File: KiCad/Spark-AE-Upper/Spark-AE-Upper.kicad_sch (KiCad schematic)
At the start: 16 parts, among them J1 SSM-120-L-SV-BE, J2 SSM-120-L-SV-BE, J3 Conn_02x05_Odd_Even, J4 Conn_02x05_Odd_Even, J5 Conn_01x08_Socket, J6 Conn_01x08_Socket, J7 USB_C_Receptacle, J8 Micro_SD_Card_Det1, SW1 SW_Push, SW2 SW_Push

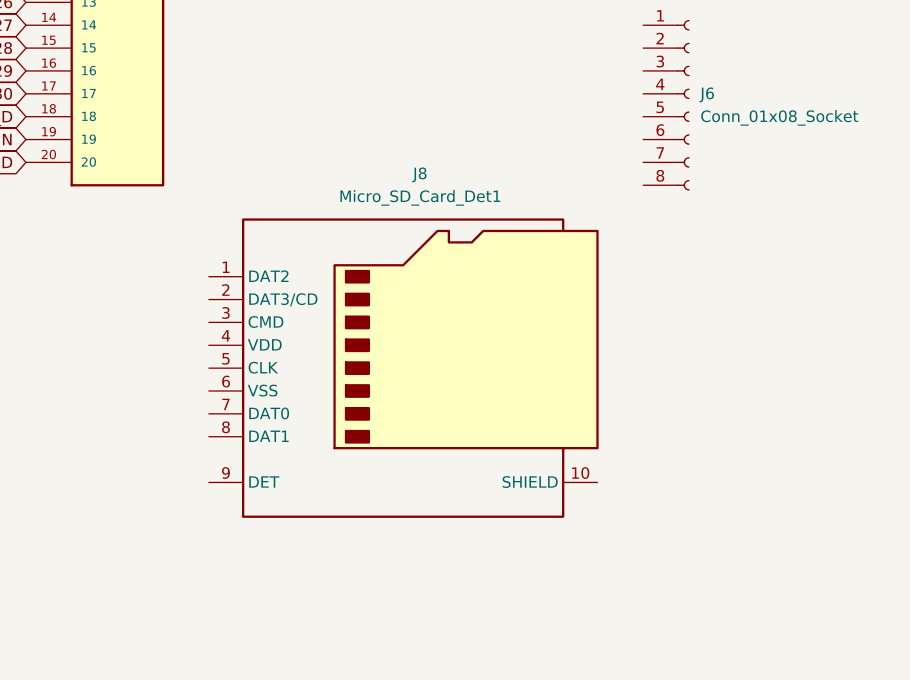
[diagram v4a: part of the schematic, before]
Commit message: updated footprints and models
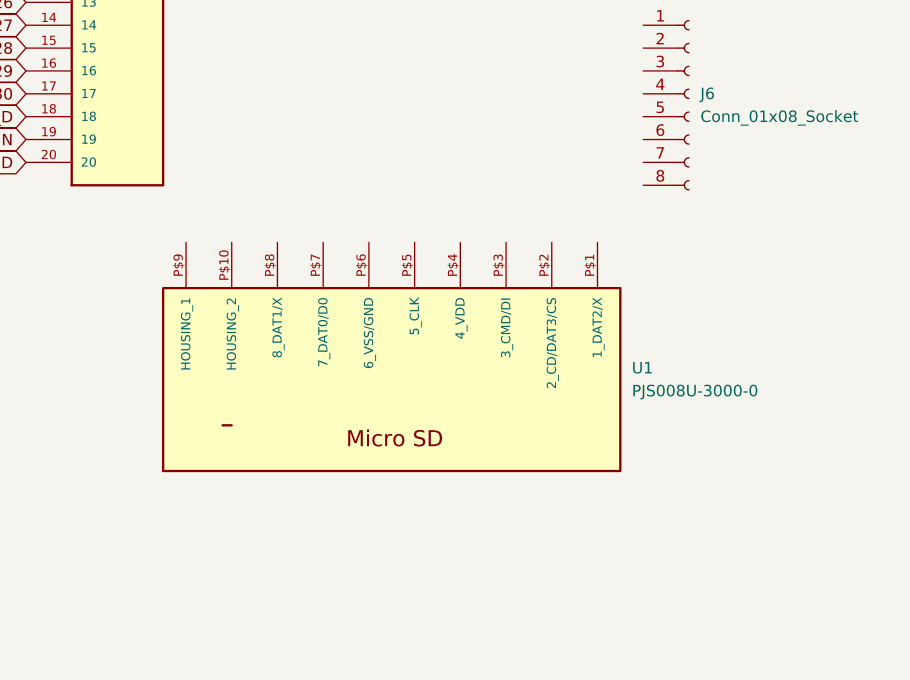
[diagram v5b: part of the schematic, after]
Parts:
- removed J8: Micro_SD_Card_Det1, Connector_Card:microSD_HC_Molex_104031-0811, symbol Connector:Micro_SD_Card_Det1
- added U1: PJS008U-3000-0, clectric-diy:PJS008U-3000-0, symbol clectric-diy:PJS008U-3000-0
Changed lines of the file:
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@@
+	)
+	(symbol
+		(lib_id "clectric-diy:PJS008U-3000-0")
+		(at 227.33 147.32 0)
+		(unit 1)
+		(exclude_from_sim no)
+		(in_bom yes)
+		(on_board yes)
+		(dnp no)
+		(fields_autoplaced yes)
+		(property "Reference" "U1"
+			(at 254 146.0499 0)
+			(effects
+				(font
+					(size 1.27 1.27)
+				)
+				(justify left)
+			)
+		)
+		(property "Value" "PJS008U-3000-0"
+			(at 254 148.5899 0)
+			(effects
+				(font
+					(size 1.27 1.27)
+				)
+				(justify left)
+			)
+		)
+		(property "Footprint" "clectric-diy:PJS008U-3000-0"
+			(at 227.33 147.32 0)
+			(effects
+				(font
+					(size 1.27 1.27)
+				)
+				(justify bottom)
+				(hide yes)
+			)
+		)
+		(property "Datasheet" ""
+			(at 227.33 147.32 0)
+			(effects
+				(font
+					(size 1.27 1.27)
+				)
+				(hide yes)
+			)
+		)
+		(property "Description" ""
+			(at 227.33 147.32 0)
+			(effects
+				(font
+					(size 1.27 1.27)
+				)
+				(hide yes)
+			)
+		)
+		(property "MF" "Yamaichi"
+			(at 227.33 147.32 0)
+			(effects
+				(font
+					(size 1.27 1.27)
+				)
+				(justify bottom)
+				(hide yes)
+			)
+		)
+		(property "Description_1" "8 Position Card Connector Secure Digital - microSD™ Through Hole Gold-Nickel"
+			(at 227.33 147.32 0)
+			(effects
+				(font
+					(size 1.27 1.27)
+				)
+				(justify bottom)
+				(hide yes)
+			)
+		)
+		(property "Package" "None"
+			(at 227.33 147.32 0)
+			(effects
+				(font
+					(size 1.27 1.27)
+				)
+				(justify bottom)
+				(hide yes)
+			)
+		)
+		(property "Price" "None"
+			(at 227.33 147.32 0)
+			(effects
+				(font
+					(size 1.27 1.27)
+				)
+				(justify bottom)
+				(hide yes)
+			)
+		)
+		(property "SnapEDA_Link" "https://www.snapeda.com/parts/PJS008U-3000-0/Yamaichi/view-part/?ref=snap"
+			(at 227.33 147.32 0)
+			(effects
+				(font
+					(size 1.27 1.27)
+				)
+				(justify bottom)
+				(hide yes)
+			)
+		)
+		(property "MP" "PJS008U-3000-0"
+			(at 227.33 147.32 0)
+			(effects
+				(font
+					(size 1.27 1.27)
+				)
+				(justify bottom)
+				(hide yes)
+			)
+		)
+		(property "Purchase-URL" "https://www.snapeda.com/api/url_track_click_mouser/?unipart_id=493587&manufacturer=Yamaichi&part_name=PJS008U-3000-0&search_term=pjs008u-3000-0"
+			(at 227.33 147.32 0)
+			(effects
+				(font
+					(size 1.27 1.27)
+				)
+				(justify bottom)
+				(hide yes)
+			)
+		)
+		(property "Availability" "In Stock"
+			(at 227.33 147.32 0)
+			(effects
+				(font
+					(size 1.27 1.27)
+				)
+				(justify bottom)
+				(hide yes)
+			)
+		)
+		(property "Check_prices" "https://www.snapeda.com/parts/PJS008U-3000-0/Yamaichi/view-part/?ref=eda"
+			(at 227.33 147.32 0)
+			(effects
+				(font
+					(size 1.27 1.27)
+				)
+				(justify bottom)
+				(hide yes)
+			)
+		)
+		(pin "P$1"
+		)
+		(pin "P$7"
+		)
+		(pin "P$5"
+		)
+		(pin "P$6"
+		)
+		(pin "P$4"
+		)
+		(pin "P$2"
+		)
+		(pin "P$3"
+		)
+		(pin "P$10"
+		)
+		(pin "P$9"
+		)
+		(pin "P$8"
+		)
+		(instances
+			(project ""
+				(path "/b249adcd-2848-4e56-9615-c4f1b6083abe"
+					(reference "U1")
+					(unit 1)
+				)
+			)
+		)
 	)
 	(symbol
@@
 					(unit 1)
 				)
-			)
-		)
-	)
-	(symbol
-		(lib_id "Connector:Micro_SD_Card_Det1")
-		(at 229.87 146.05 0)
-		(unit 1)
-		(exclude_from_sim no)
-		(in_bom yes)
-		(on_board yes)
-		(dnp no)
-		(fields_autoplaced yes)
-		(property "Reference" "J8"
-			(at 230.505 124.46 0)
-			(effects
-				(font
-					(size 1.27 1.27)
-				)
-			)
-		)
-		(property "Value" "Micro_SD_Card_Det1"
-			(at 230.505 127 0)
-			(effects
-				(font
-					(size 1.27 1.27)
-				)
-			)
-		)
-		(property "Footprint" "Connector_Card:microSD_HC_Molex_104031-0811"
-			(at 281.94 128.27 0)
-			(effects
-				(font
-					(size 1.27 1.27)
-				)
-				(hide yes)
-			)
-		)
-		(property "Datasheet" "https://datasheet.lcsc.com/lcsc/2110151630_XKB-Connectivity-XKTF-015-N_C381082.pdf"
-			(at 229.87 143.51 0)
-			(effects
-				(font
-					(size 1.27 1.27)
-				)
-				(hide yes)
-			)
-		)
-		(property "Description" "Micro SD Card Socket with one card detection pin"
-			(at 229.87 146.05 0)
-			(effects
-				(font
-					(size 1.27 1.27)
-				)
-				(hide yes)
-			)
-		)
-		(pin "6"
-		)
-		(pin "7"
-		)
-		(pin "3"
-		)
-		(pin "2"
-		)
-		(pin "4"
-		)
-		(pin "5"
-		)
-		(pin "1"
-		)
-		(pin "10"
-		)
-		(pin "9"
-		)
-		(pin "8"
-		)
-		(instances
-			(project ""
-				(path "/b249adcd-2848-4e56-9615-c4f1b6083abe"
-					(reference "J8")
-					(unit 1)
-				)

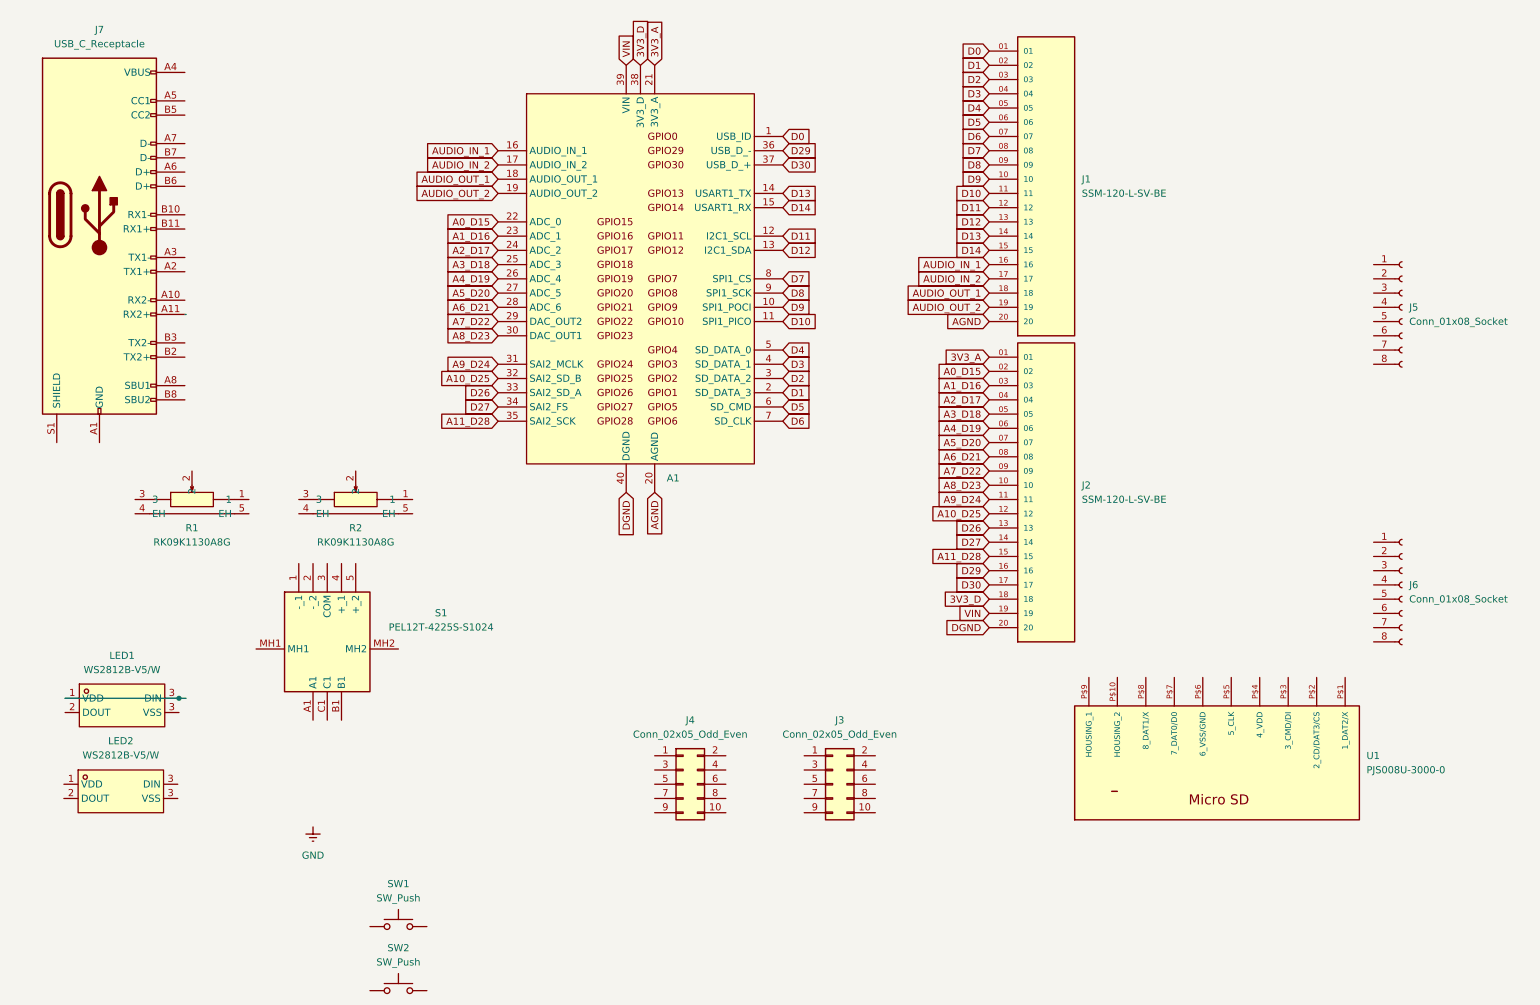
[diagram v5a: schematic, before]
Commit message: added nets for bus connectors
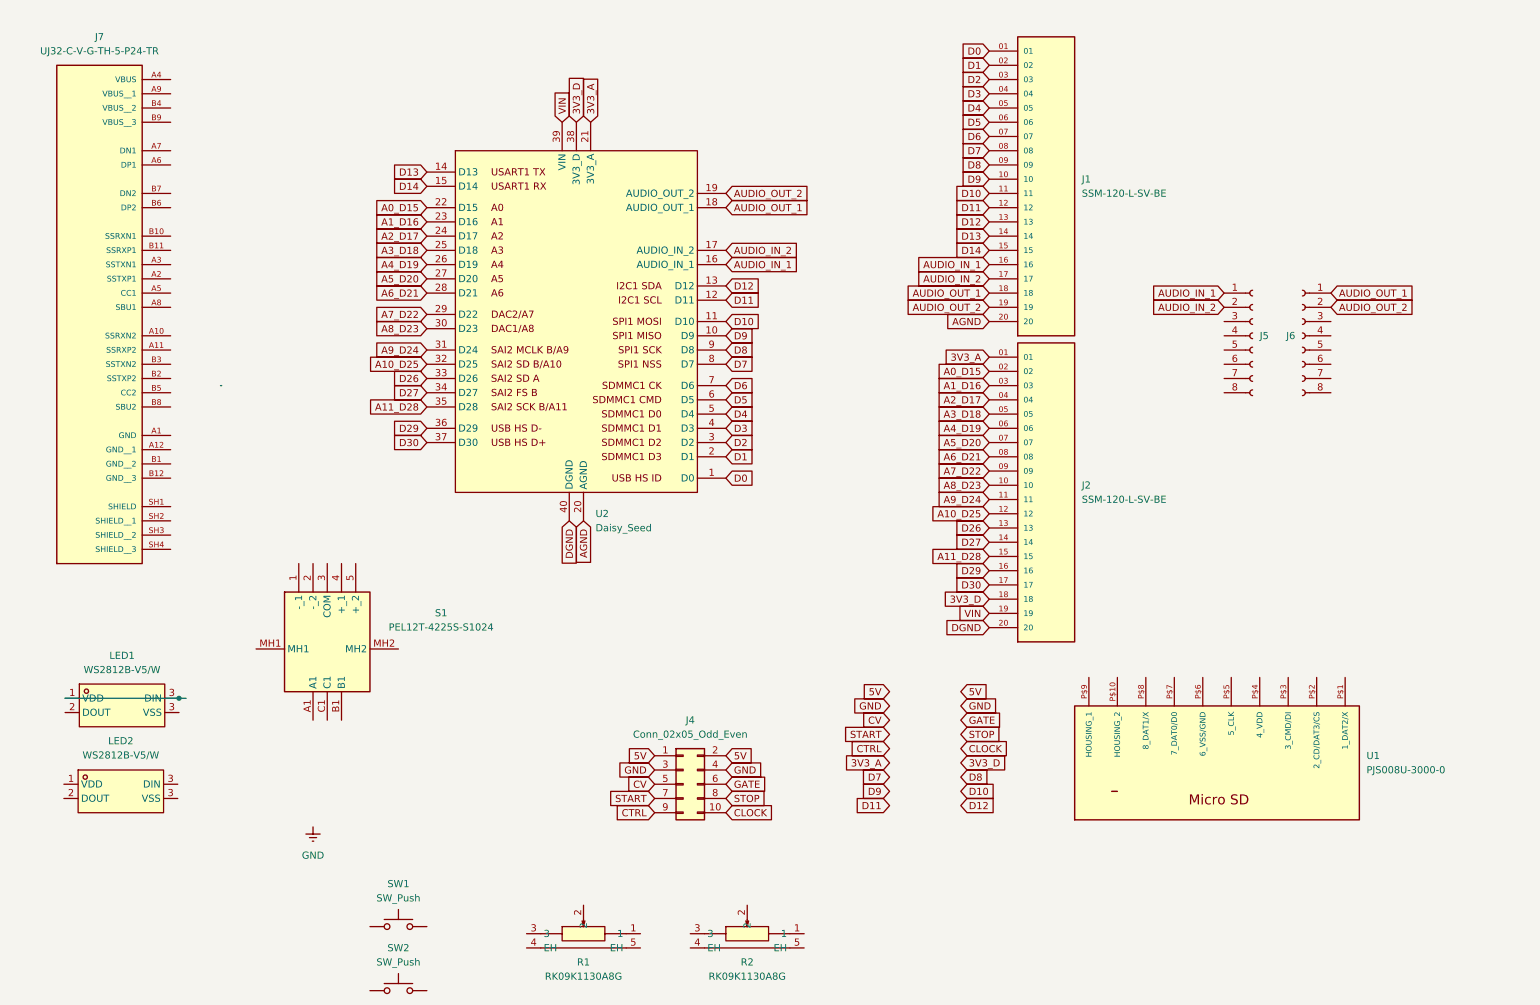
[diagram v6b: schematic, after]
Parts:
- removed A1: Electrosmith_Daisy_Seed_Rev4, Module:Electrosmith_Daisy_Seed, symbol MCU_Module:Electrosmith_Daisy_Seed_Rev4
- removed J3: Conn_02x05_Odd_Even, Connector_PinHeader_2.54mm:PinHeader_2x05_P2.54mm_Vertical, symbol Connector_Generic:Conn_02x05_Odd_Even
- removed J7: USB_C_Receptacle, Connector_USB:USB_C_Receptacle_GCT_USB4105-xx-A_16P_TopMnt_Horizontal, symbol Connector:USB_C_Receptacle
- added J7: UJ32-C-V-G-TH-5-P24-TR, clectric-diy:SAMESKY_UJ32-C-V-G-TH-5-P24-TR, symbol clectric-diy:UJ32-C-V-G-TH-5-P24-TR
- added U2: Daisy_Seed, clectric-diy:DAISY_SEED, symbol clectric-diy:Daisy_Seed
- S1: footprint PEL12T4225SS1024 -> clectric-diy:PEL12T4225SS1024
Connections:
- net 3V3_A: now also U2.21 (3V3_A)
- net 3V3_D: now also U2.38 (3V3_D)
- net A0_D15: now also U2.22 (D15)
- net A10_D25: now also U2.32 (D25)
- net A11_D28: now also U2.35 (D28)
- net A1_D16: now also U2.23 (D16)
- net A2_D17: now also U2.24 (D17)
- net A3_D18: now also U2.25 (D18)
- net A4_D19: now also U2.26 (D19)
- net A5_D20: now also U2.27 (D20)
- net A6_D21: now also U2.28 (D21)
- net A7_D22: now also U2.29 (D22)
- net A8_D23: now also U2.30 (D23)
- net A9_D24: now also U2.31 (D24)
- net AGND: now also U2.20 (AGND)
- net AUDIO_IN_1: now also J5.1 (Pin_1), U2.16 (AUDIO_IN_1)
- net AUDIO_IN_2: now also J5.2 (Pin_2), U2.17 (AUDIO_IN_2)
- net AUDIO_OUT_1: now also J6.1 (Pin_1), U2.18 (AUDIO_OUT_1)
- net AUDIO_OUT_2: now also J6.2 (Pin_2), U2.19 (AUDIO_OUT_2)
- net D0: now also U2.1 (D0)
- net D1: now also U2.2 (D1)
- net D10: now also U2.11 (D10)
- net D11: now also U2.12 (D11)
- net D12: now also U2.13 (D12)
- net D13: now also U2.14 (D13)
- net D14: now also U2.15 (D14)
- net D2: now also U2.3 (D2)
- net D26: now also U2.33 (D26)
- net D27: now also U2.34 (D27)
- net D29: now also U2.36 (D29)
- net D3: now also U2.4 (D3)
- net D30: now also U2.37 (D30)
- net D4: now also U2.5 (D4)
- net D5: now also U2.6 (D5)
- net D6: now also U2.7 (D6)
- net D7: now also U2.8 (D7)
- net D8: now also U2.9 (D8)
- net D9: now also U2.10 (D9)
- net DGND: now also U2.40 (DGND)
- net GND: now also J4.3 (Pin_3), J4.4 (Pin_4)
- net VIN: now also U2.39 (VIN)
- net 5V: now reaches J4.1 (Pin_1)
- net 5V: now also J4.2 (Pin_2)
- net CLOCK: now reaches J4.10 (Pin_10)
- net CV: now reaches J4.5 (Pin_5)
- net GATE: now reaches J4.6 (Pin_6)
- net START: now reaches J4.7 (Pin_7)
- net STOP: now reaches J4.8 (Pin_8)
- net CTRL: now reaches J4.9 (Pin_9)
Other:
- moved on the sheet: J5, J6, R1, R2

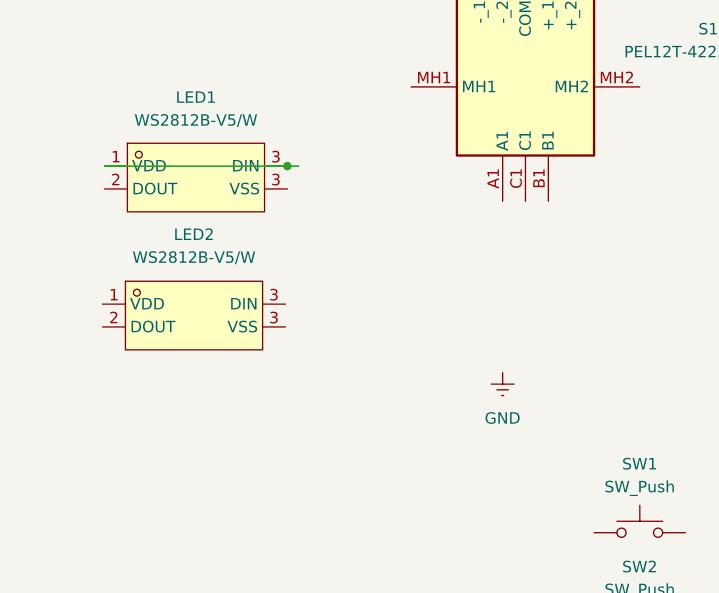
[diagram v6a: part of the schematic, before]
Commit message: added nets for ae modular i/o headers
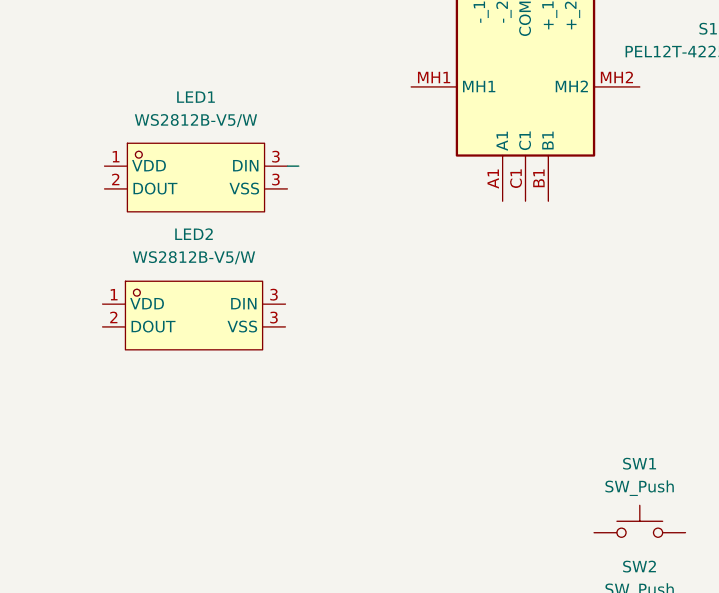
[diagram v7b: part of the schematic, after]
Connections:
- net at LED1.1 (VDD): no longer LED1.3 (VSS)
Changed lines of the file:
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@@
 		(comment 1 "Charles H. Leggett")
 	)
-	(junction
-		(at 42.1265 135.7973)
-		(diameter 0)
-		(color 0 0 0 0)
-	)
 	(wire
 		(pts
@@
 		)
 	)
-	(wire
-		(pts
-			(xy 21.8065 135.7973) (xy 42.1265 135.7973)
-		)
-		(stroke
-			(width 0)
-			(type default)
-		)
-	)
 	(global_label "A11_D28"
 		(shape input)
@@
 					(unit 1)
 				)
-			)
-		)
-	)
-	(symbol
-		(lib_id "power:GNDREF")
-		(at 66.04 158.75 0)
-		(unit 1)
-		(exclude_from_sim no)
-		(in_bom yes)
-		(on_board yes)
-		(dnp no)
-		(fields_autoplaced yes)
-		(property "Reference" "#PWR01"
-			(at 66.04 165.1 0)
-			(effects
-				(font
-					(size 1.27 1.27)
-				)
-				(hide yes)
-			)
-		)
-		(property "Value" "GND"
-			(at 66.04 163.83 0)
-			(effects
-				(font
-					(size 1.27 1.27)
-				)
-			)
-		)
-		(property "Footprint" ""
-			(at 66.04 158.75 0)
-			(effects
-				(font
-					(size 1.27 1.27)
-				)
-				(hide yes)
-			)
-		)
-		(property "Datasheet" ""
-			(at 66.04 158.75 0)
-			(effects
-				(font
-					(size 1.27 1.27)
-				)
-				(hide yes)
-			)
-		)
-		(property "Description" "Power symbol creates a global label with name \"GNDREF\" , reference supply ground"
-			(at 66.04 158.75 0)
-			(effects
-				(font
-					(size 1.27 1.27)
-				)
-				(hide yes)
-			)
-		)
-		(pin "1"
-		)
-		(instances
-			(project ""
-				(path "/b249adcd-2848-4e56-9615-c4f1b6083abe"
-					(reference "#PWR01")
-					(unit 1)
-				)
